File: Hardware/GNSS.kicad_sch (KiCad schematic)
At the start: 12 parts, among them J2 132134, U6 LM317_TO-220, U7 GK9501

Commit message: update of directory
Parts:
- renumbered C7 to C3, C4 to C8, D2 to D3, R3 to R2, R3 to R6, R5 to R8, R2 to R9, U6 to U3
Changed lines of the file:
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@@
   (symbol (lib_id "Device:R") (at 63.5 64.77 0) (unit 1)
     (in_bom yes) (on_board yes) (dnp no)
-    (property "Reference" "R5" (at 64.77 63.5 0)
+    (property "Reference" "R8" (at 64.77 63.5 0)
       (effects (font (size 1.27 1.27)) (justify left))
     )
@@
   (symbol (lib_id "power:+5V") (at 41.91 45.72 0) (unit 1)
     (in_bom yes) (on_board yes) (dnp no) (fields_autoplaced)
-    (property "Reference" "#PWR024" (at 41.91 49.53 0)
+    (property "Reference" "#PWR08" (at 41.91 49.53 0)
       (effects (font (size 1.27 1.27)) hide)
     )
@@
   (symbol (lib_id "Device:C") (at 69.85 54.61 0) (unit 1)
     (in_bom yes) (on_board yes) (dnp no)
-    (property "Reference" "C7" (at 73.66 53.34 0)
+    (property "Reference" "C3" (at 73.66 53.34 0)
       (effects (font (size 1.27 1.27)) (justify left))
     )
@@
   (symbol (lib_id "power:GND") (at 63.5 69.85 0) (unit 1)
     (in_bom yes) (on_board yes) (dnp no) (fields_autoplaced)
-    (property "Reference" "#PWR027" (at 63.5 76.2 0)
+    (property "Reference" "#PWR019" (at 63.5 76.2 0)
       (effects (font (size 1.27 1.27)) hide)
     )
@@
   (symbol (lib_id "power:GND") (at 69.85 68.58 0) (unit 1)
     (in_bom yes) (on_board yes) (dnp no) (fields_autoplaced)
-    (property "Reference" "#PWR026" (at 69.85 74.93 0)
+    (property "Reference" "#PWR020" (at 69.85 74.93 0)
       (effects (font (size 1.27 1.27)) hide)
     )
@@
   (symbol (lib_id "Device:R") (at 92.71 109.22 0) (unit 1)
     (in_bom yes) (on_board yes) (dnp no)
-    (property "Reference" "R3" (at 93.98 106.68 0)
+    (property "Reference" "R2" (at 93.98 106.68 0)
       (effects (font (size 1.27 1.27)) (justify left))
     )
@@
   (symbol (lib_id "Regulator_Linear:LM317_TO-220") (at 52.07 49.53 0) (unit 1)
     (in_bom yes) (on_board yes) (dnp no) (fields_autoplaced)
-    (property "Reference" "U6" (at 52.07 43.18 0)
+    (property "Reference" "U3" (at 52.07 43.18 0)
       (effects (font (size 1.27 1.27)))
     )
@@
   (symbol (lib_id "power:GND") (at 95.25 58.42 0) (unit 1)
     (in_bom yes) (on_board yes) (dnp no) (fields_autoplaced)
-    (property "Reference" "#PWR023" (at 95.25 64.77 0)
+    (property "Reference" "#PWR021" (at 95.25 64.77 0)
       (effects (font (size 1.27 1.27)) hide)
     )
@@
   (symbol (lib_id "Device:R") (at 63.5 54.61 0) (unit 1)
     (in_bom yes) (on_board yes) (dnp no)
-    (property "Reference" "R3" (at 64.77 52.07 0)
+    (property "Reference" "R6" (at 64.77 52.07 0)
       (effects (font (size 1.27 1.27)) (justify left))
     )
@@
   (symbol (lib_id "Device:C") (at 95.25 54.61 0) (unit 1)
     (in_bom yes) (on_board yes) (dnp no) (fields_autoplaced)
-    (property "Reference" "C4" (at 99.06 53.34 0)
+    (property "Reference" "C8" (at 99.06 53.34 0)
       (effects (font (size 1.27 1.27)) (justify left))
     )
@@
   (symbol (lib_id "Device:R") (at 90.17 49.53 90) (unit 1)
     (in_bom yes) (on_board yes) (dnp no) (fields_autoplaced)
-    (property "Reference" "R2" (at 90.17 43.18 90)
+    (property "Reference" "R9" (at 90.17 43.18 90)
       (effects (font (size 1.27 1.27)))
     )
@@
   (symbol (lib_id "Device:D") (at 76.2 49.53 180) (unit 1)
     (in_bom yes) (on_board yes) (dnp no) (fields_autoplaced)
-    (property "Reference" "D2" (at 76.2 43.18 0)
-      (effects (font (size 1.27 1.27)))
-    )
+    (property "Reference" "D3" (at 76.2 43.18 0)
+      (effects (font (size 1.27 1.27)))
+    )

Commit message: Update of PCB
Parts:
- added C10: 100nF, Capacitor_THT:C_Rect_L7.0mm_W2.0mm_P5.00mm, symbol Device:C
- D2, D3: value D -> 1N4818
- R2, R3, R6, R8, R9: footprint Resistor_THT:R_Axial_DIN0204_L3.6mm_D1.6mm_P5.08mm_Horizontal -> Resistor_THT:R_Axial_DIN0207_L6.3mm_D2.5mm_P7.62mm_Horizontal
- renumbered J2 to J10
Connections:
- net +5V: now also C10.1
- net GND: now also C10.2
- no-connect marks 11 -> 12
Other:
- moved on the sheet: C8

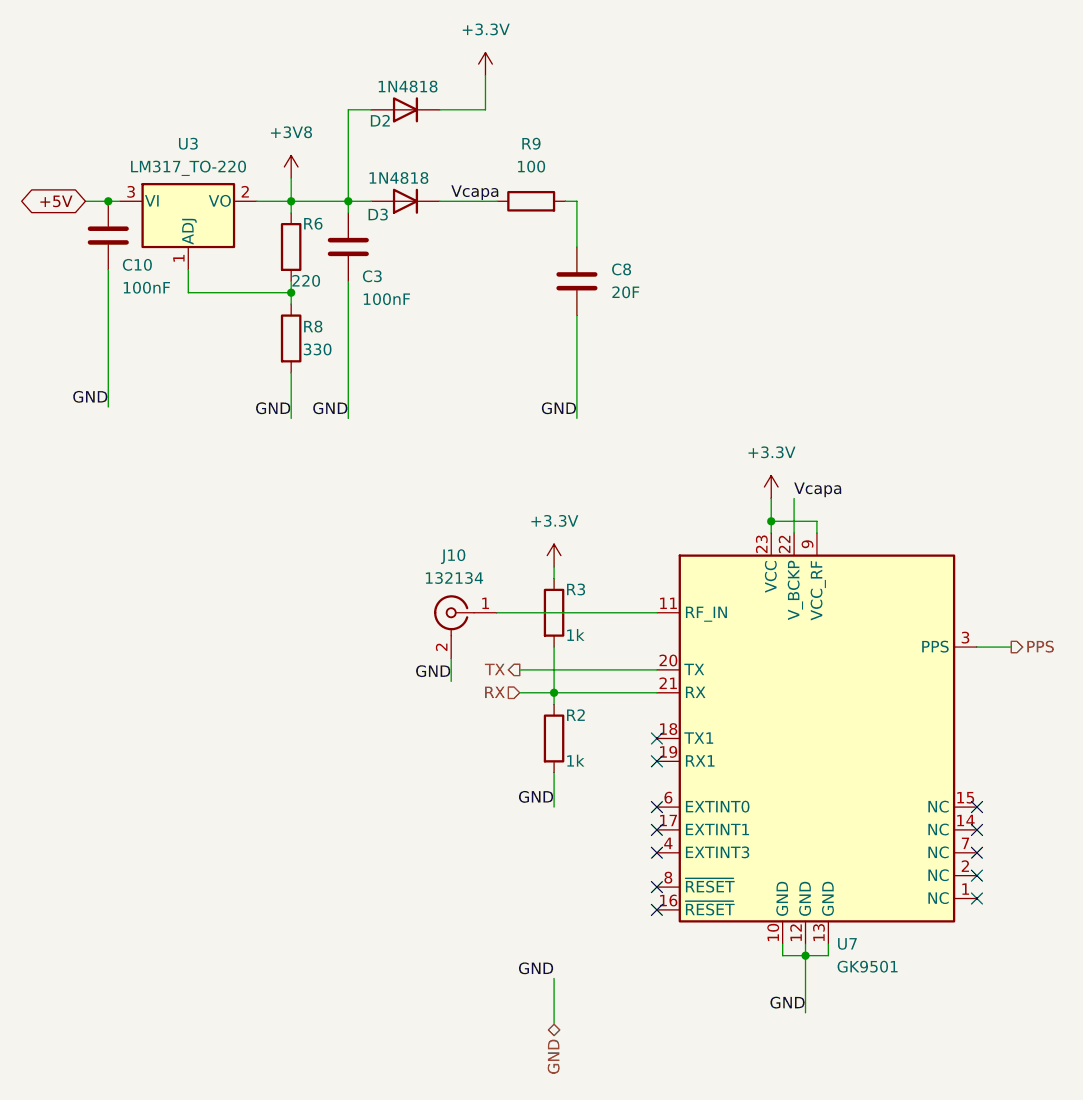
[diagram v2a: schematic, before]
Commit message: Update PCB of Motor controller - version sent on production (debug purpose)
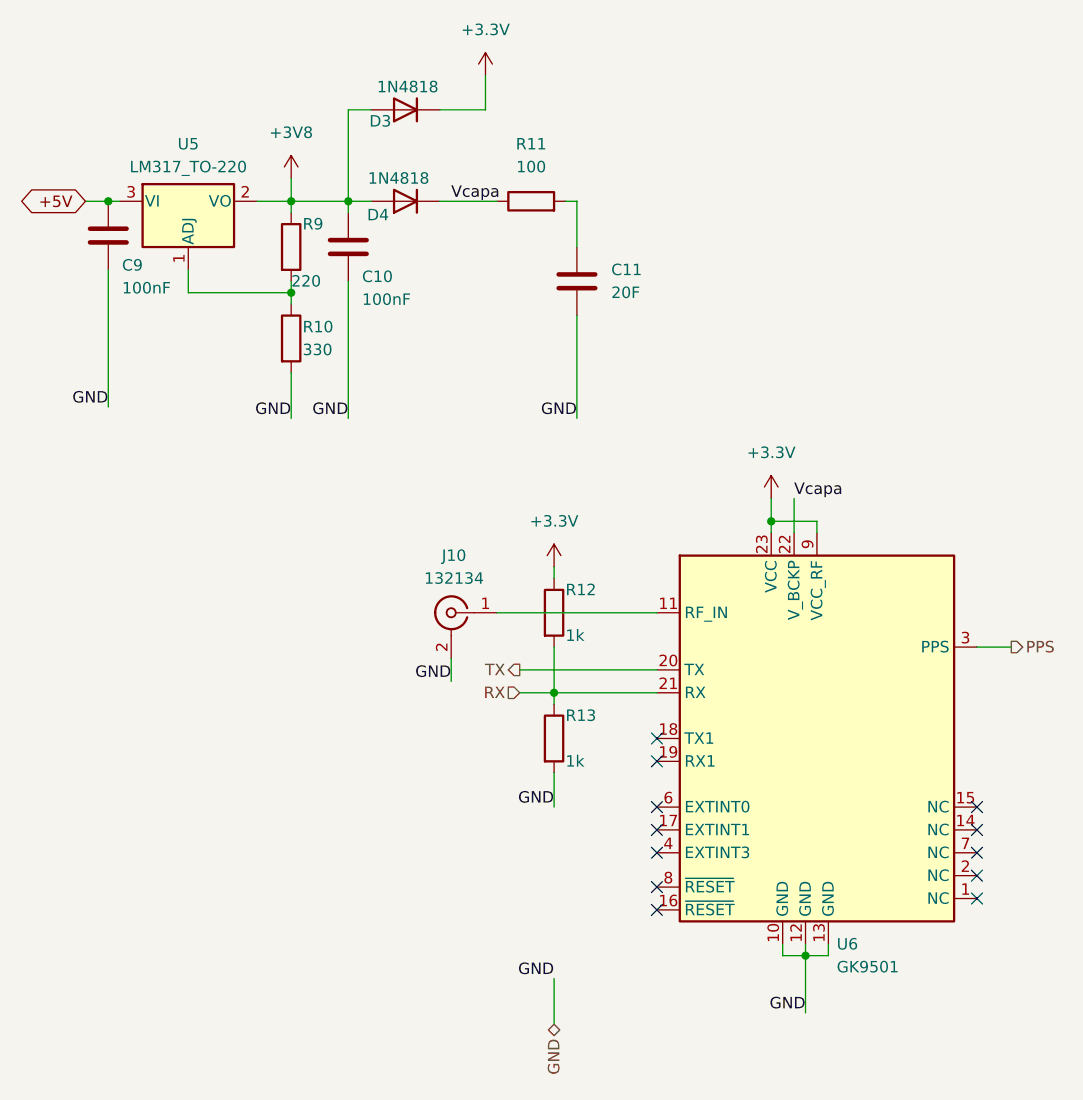
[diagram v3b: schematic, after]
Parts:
- renumbered C3 to C10, C8 to C11, C10 to C9, D2 to D3, D3 to D4, R8 to R10, R9 to R11, R3 to R12, R2 to R13, R6 to R9, U3 to U5, U7 to U6
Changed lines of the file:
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@@
 		(on_board yes)
 		(dnp no)
-		(property "Reference" "R8"
+		(property "Reference" "R10"
 			(at 64.77 63.5 0)
 			(effects
@@
 			(project "Tracker"
 				(path "/60c5e70b-bc37-4402-aa86-9378cecb8f85/9a9cee9e-b09b-4eb3-a522-35ab2aca519e"
-					(reference "R8")
+					(reference "R10")
 					(unit 1)
 				)
@@
 		(dnp no)
 		(fields_autoplaced yes)
-		(property "Reference" "#PWR027"
+		(property "Reference" "#PWR028"
 			(at 92.71 93.98 0)
 			(effects
@@
 			(project "Tracker"
 				(path "/60c5e70b-bc37-4402-aa86-9378cecb8f85/9a9cee9e-b09b-4eb3-a522-35ab2aca519e"
-					(reference "#PWR027")
+					(reference "#PWR028")
 					(unit 1)
 				)
@@
 		(on_board yes)
 		(dnp no)
-		(property "Reference" "C3"
+		(property "Reference" "C10"
 			(at 71.374 57.912 0)
 			(effects
@@
 			(project "Tracker"
 				(path "/60c5e70b-bc37-4402-aa86-9378cecb8f85/9a9cee9e-b09b-4eb3-a522-35ab2aca519e"
-					(reference "C3")
+					(reference "C10")
 					(unit 1)
 				)
@@
 		(dnp no)
 		(fields_autoplaced yes)
-		(property "Reference" "#PWR022"
+		(property "Reference" "#PWR026"
 			(at 63.5 50.8 0)
 			(effects
@@
 			(project "Tracker"
 				(path "/60c5e70b-bc37-4402-aa86-9378cecb8f85/9a9cee9e-b09b-4eb3-a522-35ab2aca519e"
-					(reference "#PWR022")
+					(reference "#PWR026")
 					(unit 1)
 				)
@@
 		(dnp no)
 		(fields_autoplaced yes)
-		(property "Reference" "#PWR024"
+		(property "Reference" "#PWR029"
 			(at 116.84 86.36 0)
 			(effects
@@
 			(project "Tracker"
 				(path "/60c5e70b-bc37-4402-aa86-9378cecb8f85/9a9cee9e-b09b-4eb3-a522-35ab2aca519e"
-					(reference "#PWR024")
+					(reference "#PWR029")
 					(unit 1)
 				)
@@
 		(on_board yes)
 		(dnp no)
-		(property "Reference" "C10"
+		(property "Reference" "C9"
 			(at 44.704 56.642 0)
 			(effects
@@
 			(project "Tracker"
 				(path "/60c5e70b-bc37-4402-aa86-9378cecb8f85/9a9cee9e-b09b-4eb3-a522-35ab2aca519e"
-					(reference "C10")
+					(reference "C9")
 					(unit 1)
 				)
@@
 		(dnp no)
 		(fields_autoplaced yes)
-		(property "Reference" "#PWR023"
+		(property "Reference" "#PWR027"
 			(at 85.09 39.37 0)
 			(effects
@@
 			(project "Tracker"
 				(path "/60c5e70b-bc37-4402-aa86-9378cecb8f85/9a9cee9e-b09b-4eb3-a522-35ab2aca519e"
-					(reference "#PWR023")
+					(reference "#PWR027")
 					(unit 1)
 				)
@@
 		(on_board yes)
 		(dnp no)
-		(property "Reference" "R2"
+		(property "Reference" "R13"
 			(at 93.98 106.68 0)
 			(effects
@@
 			(project "Tracker"
 				(path "/60c5e70b-bc37-4402-aa86-9378cecb8f85/9a9cee9e-b09b-4eb3-a522-35ab2aca519e"
-					(reference "R2")
+					(reference "R13")
 					(unit 1)
 				)
@@
 		(dnp no)
 		(fields_autoplaced yes)
-		(property "Reference" "U3"
+		(property "Reference" "U5"
 			(at 52.07 43.18 0)
 			(effects
@@
 			(project "Tracker"
 				(path "/60c5e70b-bc37-4402-aa86-9378cecb8f85/9a9cee9e-b09b-4eb3-a522-35ab2aca519e"
-					(reference "U3")
+					(reference "U5")
 					(unit 1)
 				)
@@
 		(on_board yes)
 		(dnp no)
-		(property "Reference" "R6"
+		(property "Reference" "R9"
 			(at 64.77 52.07 0)
 			(effects
@@
 			(project "Tracker"
 				(path "/60c5e70b-bc37-4402-aa86-9378cecb8f85/9a9cee9e-b09b-4eb3-a522-35ab2aca519e"
-					(reference "R6")
+					(reference "R9")
 					(unit 1)
 				)
@@
 		(dnp no)
 		(fields_autoplaced yes)
-		(property "Reference" "C8"
+		(property "Reference" "C11"
 			(at 99.06 57.15 0)
 			(effects
@@
 			(project "Tracker"
 				(path "/60c5e70b-bc37-4402-aa86-9378cecb8f85/9a9cee9e-b09b-4eb3-a522-35ab2aca519e"
-					(reference "C8")
+					(reference "C11")
 					(unit 1)
 				)
@@
 		(dnp no)
 		(fields_autoplaced yes)
-		(property "Reference" "R9"
+		(property "Reference" "R11"
 			(at 90.17 43.18 90)
 			(effects
@@
 			(project "Tracker"
 				(path "/60c5e70b-bc37-4402-aa86-9378cecb8f85/9a9cee9e-b09b-4eb3-a522-35ab2aca519e"
-					(reference "R9")
+					(reference "R11")
 					(unit 1)
 				)
@@
 		(dnp no)
 		(fields_autoplaced yes)
-		(property "Reference" "U7"
+		(property "Reference" "U6"
 			(at 124.1141 132.08 0)
 			(effects
@@
 			(project "Tracker"
 				(path "/60c5e70b-bc37-4402-aa86-9378cecb8f85/9a9cee9e-b09b-4eb3-a522-35ab2aca519e"
-					(reference "U7")
+					(reference "U6")
 					(unit 1)
 				)
@@
 		(on_board yes)
 		(dnp no)
-		(property "Reference" "D2"
+		(property "Reference" "D3"
 			(at 73.406 40.64 0)
 			(effects
@@
 			(project "Tracker"
 				(path "/60c5e70b-bc37-4402-aa86-9378cecb8f85/9a9cee9e-b09b-4eb3-a522-35ab2aca519e"
-					(reference "D2")
+					(reference "D3")
 					(unit 1)
 				)
@@
 		(on_board yes)
 		(dnp no)
-		(property "Reference" "R3"
+		(property "Reference" "R12"
 			(at 93.98 92.71 0)
 			(effects
@@
 			(project "Tracker"
 				(path "/60c5e70b-bc37-4402-aa86-9378cecb8f85/9a9cee9e-b09b-4eb3-a522-35ab2aca519e"
-					(reference "R3")
+					(reference "R12")
 					(unit 1)
 				)
@@
 		(on_board yes)
 		(dnp no)
-		(property "Reference" "D3"
+		(property "Reference" "D4"
 			(at 73.152 51.054 0)
 			(effects
@@
 			(project "Tracker"
 				(path "/60c5e70b-bc37-4402-aa86-9378cecb8f85/9a9cee9e-b09b-4eb3-a522-35ab2aca519e"
-					(reference "D3")
-					(unit 1)
-				)
+					(reference "D4")
+					(unit 1)
+				)
